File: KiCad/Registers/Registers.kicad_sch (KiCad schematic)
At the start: 29 parts, among them J1 TO_BACKPLANE, J2 ACCUMULATOR_OUT, J3 FROM_CTRL, J4 TO_MEMORY, J5 TO_FP, U31 74HC74, U32 74HCT32, U37 74HC688, U38 74HC688, U39 74HC688, U40 74HC688, U46 74HC244, U47 74HC244, U48 74HC244, U50 74AHC1G04

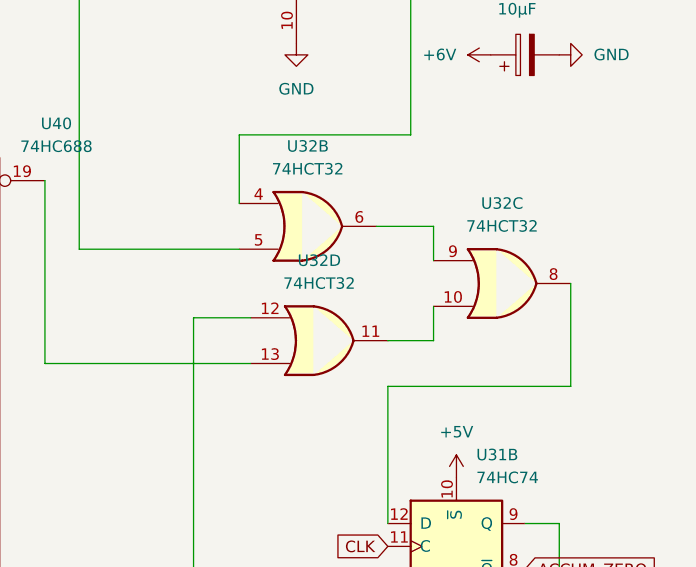
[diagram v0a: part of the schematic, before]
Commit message: Simple bootloader program.
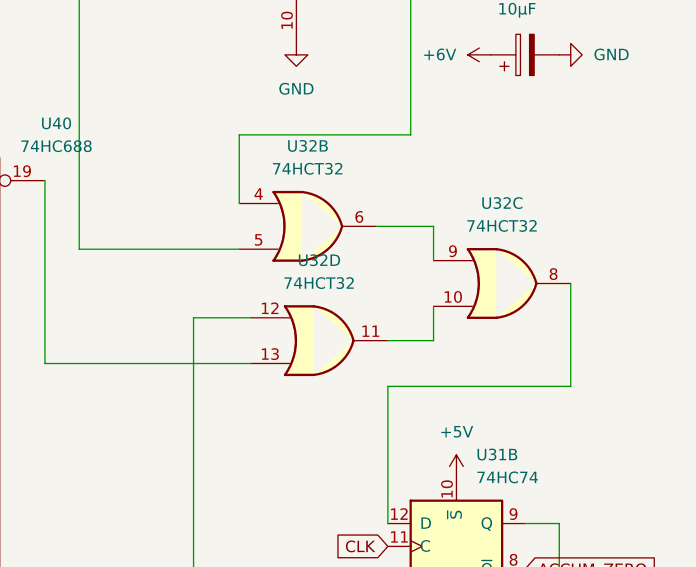
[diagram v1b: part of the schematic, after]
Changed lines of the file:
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@@
 (kicad_sch
-	(version 20231120)
+	(version 20250114)
 	(generator "eeschema")
-	(generator_version "8.0")
+	(generator_version "9.0")
 	(paper "A4")
+	(text "Make A25 LED different color on FP"
+		(exclude_from_sim no)
+		(at 115.824 105.156 0)
+		(effects
+			(font
+				(size 1.27 1.27)
+			)
+		)
+	)
+	(text "Make sure H_CYC_1 has a strong drive"
+		(exclude_from_sim no)
+		(at 84.836 81.534 0)
+		(effects
+			(font
+				(size 1.27 1.27)
+			)
+		)
+	)
 	(junction
 		(at 185.42 73.66)
@@
 		)
 	)
-	(text "Make A25 LED different color on FP"
-		(exclude_from_sim no)
-		(at 115.824 105.156 0)
-		(effects
-			(font
-				(size 1.27 1.27)
-			)
-		)
-	)
-	(text "Make sure H_CYC_1 has a strong drive"
-		(exclude_from_sim no)
-		(at 84.836 81.534 0)
-		(effects
-			(font
-				(size 1.27 1.27)
-			)
-		)
-	)
 	(global_label "BUFF_A4"
 		(shape input)
@@
 		(at 133.35 34.29)
 		(size 30.48 20.32)
+		(exclude_from_sim no)
+		(in_bom yes)
+		(on_board yes)
+		(dnp no)
 		(fields_autoplaced yes)
 		(stroke
@@
 		(at 127 69.85)
 		(size 39.37 22.86)
+		(exclude_from_sim no)
+		(in_bom yes)
+		(on_board yes)
+		(dnp no)
 		(fields_autoplaced yes)
 		(stroke
@@
 		(at 101.6 63.5)
 		(size 15.24 12.7)
+		(exclude_from_sim no)
+		(in_bom yes)
+		(on_board yes)
+		(dnp no)
 		(fields_autoplaced yes)
 		(stroke
@@
 		)
 	)
+	(embedded_fonts no)
 )

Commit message: Update schematics with fixes.
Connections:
- net H_CYC_1 is gone; now on net GND: J3.10 (Pin_10)
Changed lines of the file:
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@@
 		)
 	)
-	(global_label "H_CYC_1"
-		(shape input)
-		(at 82.55 101.6 0)
-		(fields_autoplaced yes)
-		(effects
-			(font
-				(size 1.27 1.27)
-			)
-			(justify left)
-		)
-		(property "Intersheetrefs" "${INTERSHEET_REFS}"
-			(at 93.639 101.6 0)
-			(effects
-				(font
-					(size 1.27 1.27)
-				)
-				(justify left)
-				(hide yes)
-			)
-		)
-	)
 	(global_label "DB9"
 		(shape input)
@@
 					(unit 1)
 				)
+			)
+		)
+	)
+	(symbol
+		(lib_id "power:GND")
+		(at 82.55 101.6 90)
+		(unit 1)
+		(exclude_from_sim no)
+		(in_bom yes)
+		(on_board yes)
+		(dnp no)
+		(fields_autoplaced yes)
+		(property "Reference" "#PWR0210"
+			(at 88.9 101.6 0)
+			(effects
+				(font
+					(size 1.27 1.27)
+				)
+				(hide yes)
+			)
+		)
+		(property "Value" "GND"
+			(at 86.36 101.5999 90)
+			(effects
+				(font
+					(size 1.27 1.27)
+				)
+				(justify right)
+			)
+		)
+		(property "Footprint" ""
+			(at 82.55 101.6 0)
+			(effects
+				(font
+					(size 1.27 1.27)
+				)
+				(hide yes)
+			)
+		)
+		(property "Datasheet" ""
+			(at 82.55 101.6 0)
+			(effects
+				(font
+					(size 1.27 1.27)
+				)
+				(hide yes)
+			)
+		)
+		(property "Description" "Power symbol creates a global label with name \"GND\" , ground"
+			(at 82.55 101.6 0)
+			(effects
+				(font
+					(size 1.27 1.27)
+				)
+				(hide yes)
+			)
+		)
+		(pin "1"
+		)
+		(instances
+			(project "Registers"
+				(path "/bb2d8093-1baa-42e1-9f61-d1b3316cfdc8"
+					(reference "#PWR0210")
+					(unit 1)
+				)
